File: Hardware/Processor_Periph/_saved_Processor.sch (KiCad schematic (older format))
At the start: 115 parts, among them J1 5V, J2 UART0, J3 USB_OTG, J4 JTAGICE3-SWD, Q1 BSS806NE, Q2 BSS806NE, Q3 BSS806NE, Q4 BSS806NE, SW1 PB, SW2 PB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

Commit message: Selected Ethernet PHY
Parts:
- added C?: 10uF, Capacitors_SMD:C_0805, symbol C
- added C? (x3): 100nF, Capacitors_SMD:C_0603, symbol C
- added J?: RJ45-TRANSFO, symbol RJ45-TRANSFO
- added R?: 4.87k, symbol R
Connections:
- net GND: now also C?.2, C?.2, C?.2, C?.2
- net at U?.18 (PFBIN1): now also C?.1
- net at U?.23 (PFBOUT): now also C?.1, C?.1
- net at U?.37 (PFBIN2): now also C?.1

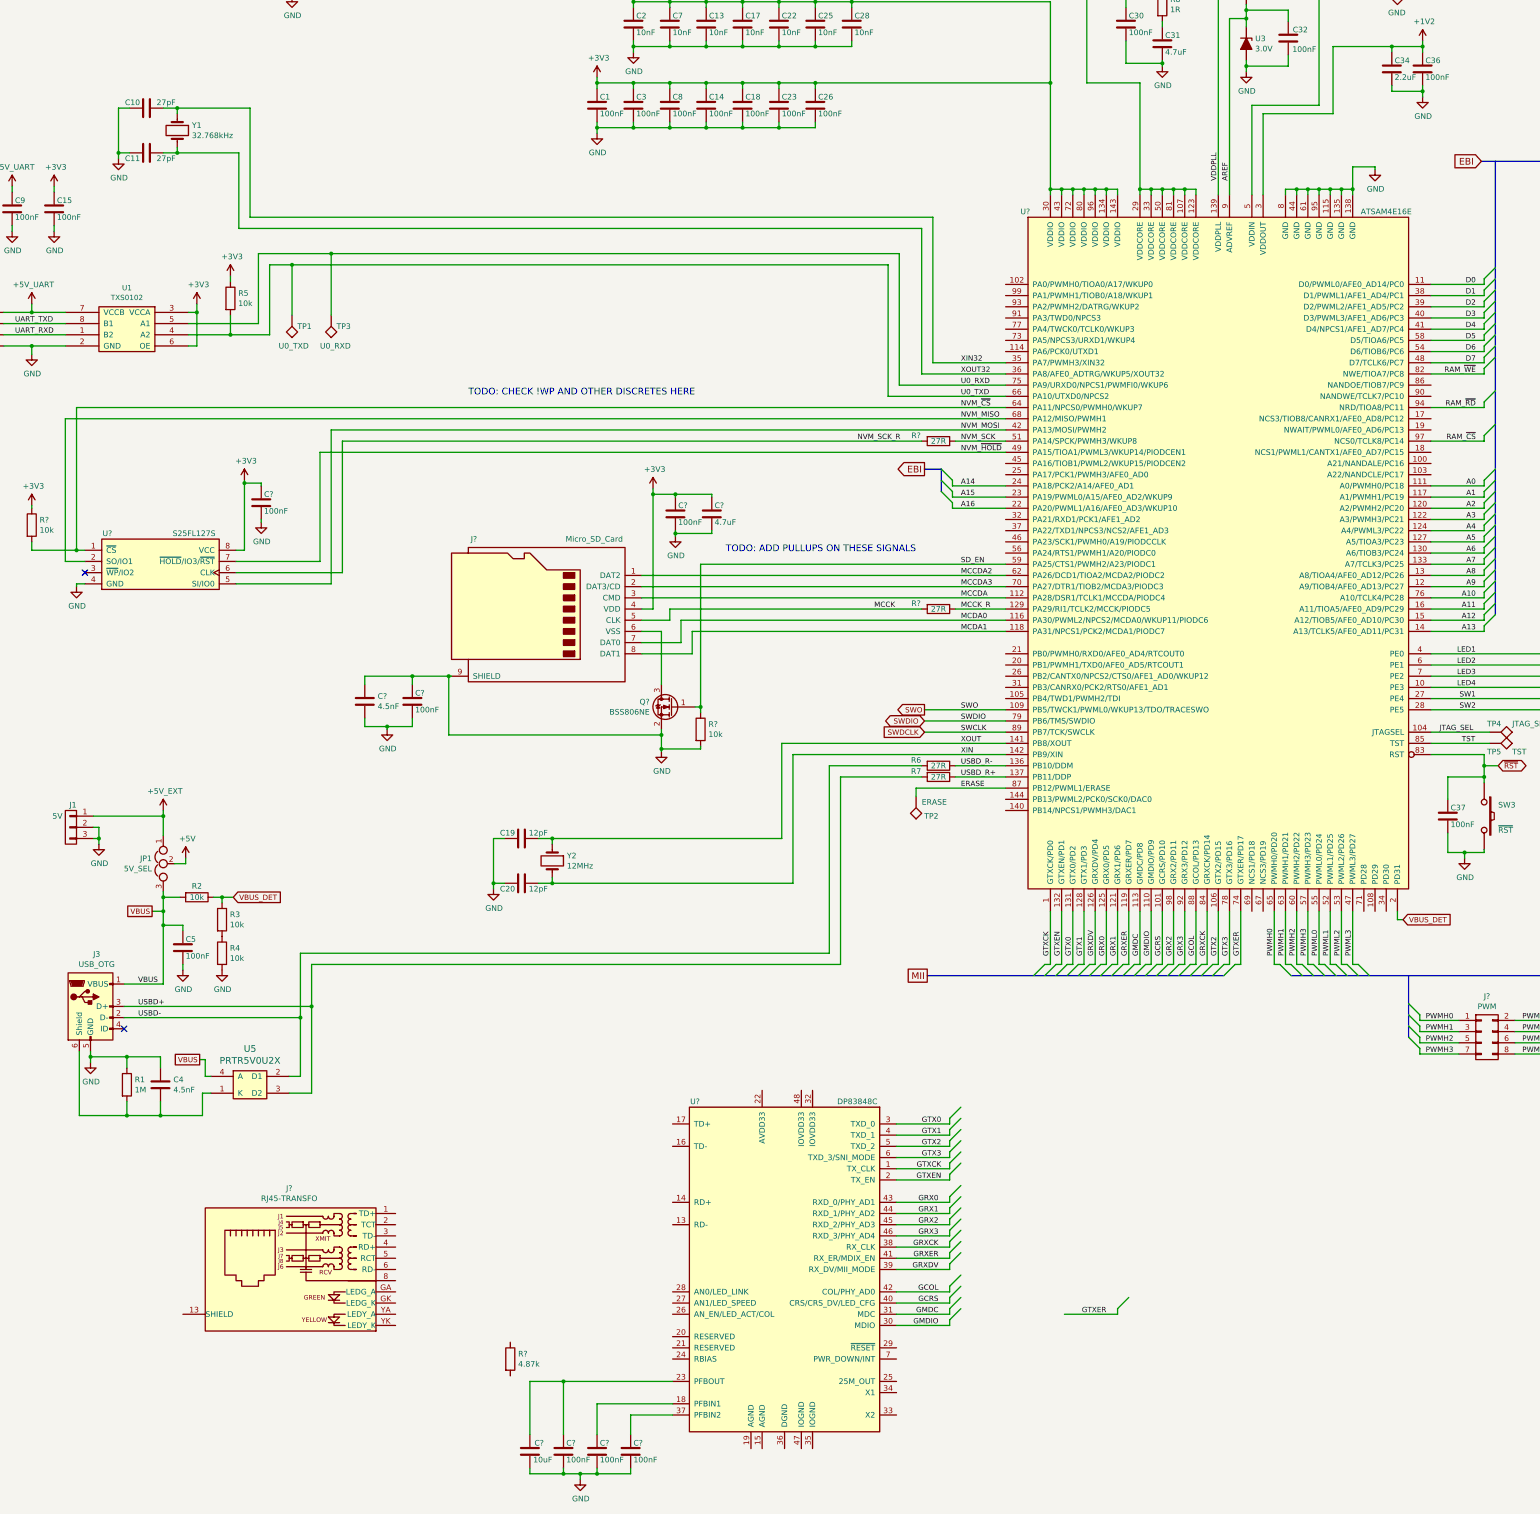
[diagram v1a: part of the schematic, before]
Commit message: Added design_notes and preliminary KiCad style guide
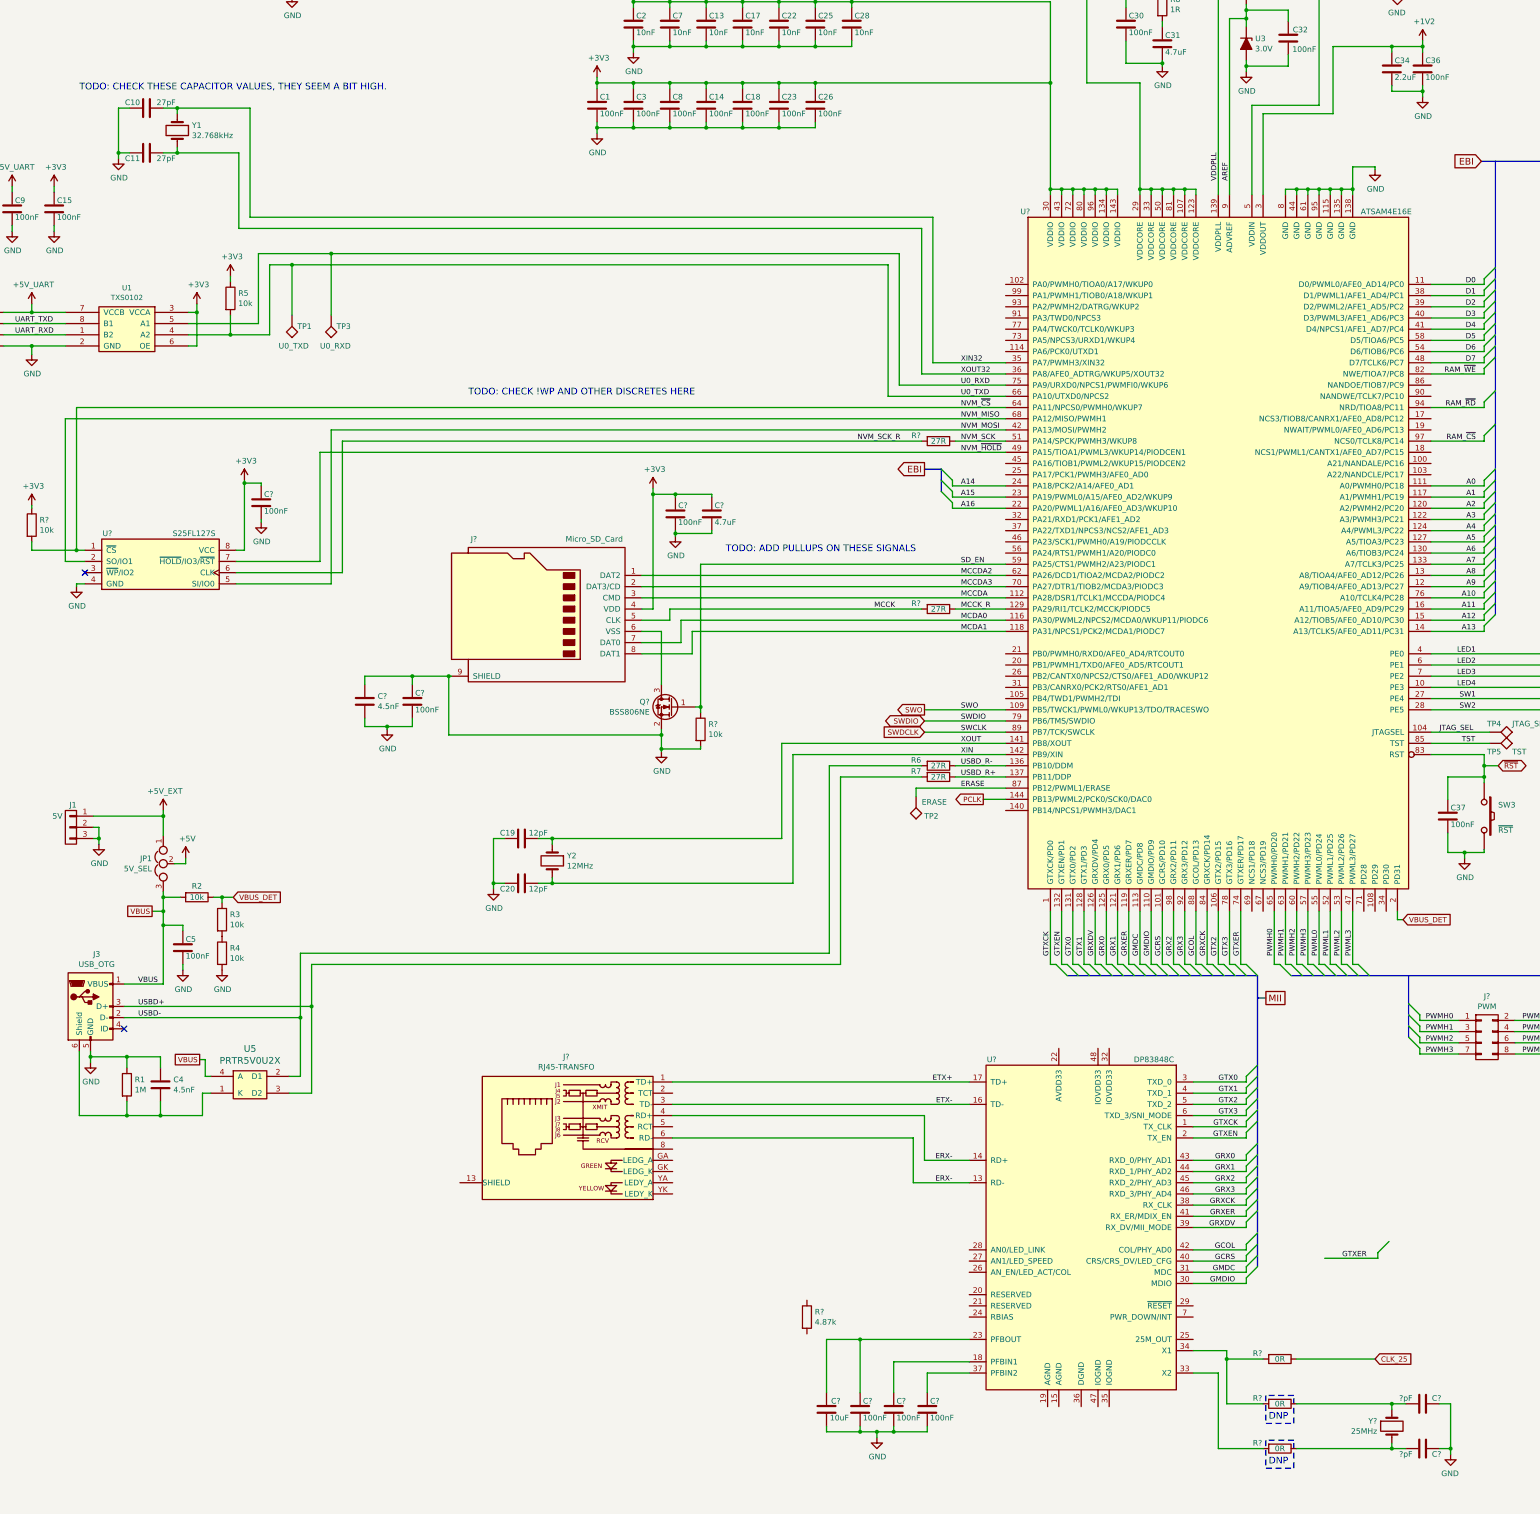
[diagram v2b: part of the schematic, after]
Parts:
- added C? (x2): ?pF, Capacitors_SMD:C_0603, symbol C
- added R? (x3): 0R, Capacitors_SMD:C_0603, symbol R
- added Y?: 25MHz, Crystals:Crystal_HC49-SD_SMD, symbol Crystal
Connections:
- net GND: now also C?.2, C?.2
- net PCLK: now reaches U?.144 (PB13/PWML2/PCK0/SCK0/DAC0)
- net ERX-: now reaches U?.13 (RD-)
- net ERX-: now also J?.4 (RD+), J?.6 (RD-), U?.14 (RD+)
- net ETX-: now reaches U?.16 (TD-)
- net ETX-: now also J?.3 (TD-)
- net ETX+: now reaches U?.17 (TD+)
- net ETX+: now also J?.1 (TD+)
- net at U?.33 (X2): now also R?.2
- net at U?.34 (X1): now also R?.2, R?.2
- new net: C?.1, R?.1, Y?.1
- new net: C?.1, R?.1, Y?.2
- new net CLK_25: R?.1
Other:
- note added: "DNP"
- note added: "TODO: CHECK THESE CAPACITOR VALUES, THEY SEEM A BIT HIGH."
- moved on the sheet: C?, J?, R?, U?
